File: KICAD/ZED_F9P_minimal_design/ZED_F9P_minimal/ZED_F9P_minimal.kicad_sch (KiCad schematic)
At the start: 2 parts, among them IC1 ZED-F9P-15B

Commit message: Update ZED_F9P_minimal.kicad_sch
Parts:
- added AE1: Antenna_Shield, symbol Device:Antenna_Shield
- added C2: 100nf_16V, symbol Device:C
- added C3: 11pF, symbol Device:C
- added C4: 1µF, Capacitor_SMD:C_0201_0603Metric, symbol Device:C
- added D1: LED, symbol Device:LED
- added D2: D_Zener, symbol Device:D_Zener
- added D3: D_TVS, symbol Device:D_TVS
- added FB1: 120ohm 300mA, symbol Device:FerriteBead
- added L1: 0.01 µH, symbol Device:L
- added R1: 10 Ohm, symbol Device:R
- added R2: 8.2ohm, symbol Device:R
- added R3: R, symbol Device:R
- added U1: NCV8705ML33TCG, DFNW8-3x3_ONS, symbol Voltage regulator:NCV8705ML33TCG
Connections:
- net +3.3V: now also FB1.2, U1.5 (EN), U1.8 (IN); no longer IC1.33 (VCC_1), IC1.34 (VCC_2), IC1.36 (V_BCKP)
- net GND: now also AE1.2 (Shield), C2.2, C3.2, C4.2, D1.1 (K), D2.2 (A), D3.1 (A1), U1.4 (GND)
- net at IC1.20 (RTK_STAT): now also R3.2
- net at IC1.39 (USB_DM): now also IC1.40 (USB_DP)
- net Antenna: no longer names the net of IC1.2 (RF_IN)
- net Antenna: now also C3.1, R2.2
- new net: D1.2 (A), R3.1
- new net: AE1.1 (A), D2.1 (K), D3.2 (A2), L1.1, R2.1
- new net: C4.1, IC1.33 (VCC_1), IC1.34 (VCC_2), U1.1 (OUT)
- new net: C2.1, L1.2, R1.2
- new net: FB1.1, R1.1
- no-connect marks 0 -> 29
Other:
- note added: "(input/output)- USB DATA"
- note added: "-output Sortie timer (si on veut ssynchro des choses dessus)"
- note added: "D_SEL=1 I2C_DATA / D_SEL=0 SPI Chip Select (Input/Output)- D_SEL=1 I2C_CLK / D_SEL=0 SPI_CLK (Input/Output)-"
- note added: "Etat du registre TX output- (cf p.87)buffer full ou ready for data"
- note added: "RESET du F9P, supr ttes les infos et cold start,en dernier recours uniquement input- état bas pdt 100ms pour trigger le reset"
- note added: "adaptation alimentation"
- note added: "détermination de D_SEL (input)-"
- note added: "filtre RC 1.76GHz"
- note added: "input UART from chip output"
- note added: "output- D_SEL=0 SPI_SD D_SEL=1 UART from host input-"
- note added: "protections ESD"
- note added: "statut RTK : off = fixed clignote = reçois/corrige on = pas de corrections"
- note removed: "IL faut proteger l'antenne ESD"
- moved on the sheet: IC1

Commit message: work on schematic and footprint
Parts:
- removed AE1: Antenna_Shield, symbol Device:Antenna_Shield
- removed FB1: 120ohm 300mA, symbol Device:FerriteBead
- added C5: 2µF, 2_2uF:CAPC1608X90, symbol Device:C
- added J1: Conn_Coaxial_Small, SMA:RFSOLUTIONS_CON-SMA-EDGE-S, symbol Connector:Conn_Coaxial_Small
- added R4: 120, symbol Device:R
- C1, C4: footprint Capacitor_SMD:C_0201_0603Metric -> 1uF:YAG_CC0603_YAG
- C2: footprint (none) -> 0_1uF:YAG_CC0603_YAG
- C3: footprint (none) -> 11pF:CAPC1608X90
- D1: value LED -> EASR3216RA0
- L1: footprint (none) -> 0_01uH:STA_RMCF1206_STP
- R1, R2: footprint (none) -> 10_Ohm:RC0402N_YAG
- R3: value R -> 330
- U1: footprint DFNW8-3x3_ONS -> LM5168F:DFNW8-3x3_ONS
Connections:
- net +3.3V: now also IC1.36 (V_BCKP), C5.1
- net GND: now also C5.2, J1.2 (Ext), R4.2
- net at D1.2 (A), R3.1: now also R4.1
- net RF_IN: now reaches D2.1 (K), D3.2 (A2), L1.1, R2.1
- net RF_IN: now also C3.1, IC1.2 (RF_IN), R2.2, J1.1 (In)
- net UART_RX: now reaches IC1.26 (RXD2)
- net UART_TX: now reaches IC1.27 (TXD2)
- net TIMER: now reaches IC1.53 (TIMEPULSE)
- net VCC_RF: now reaches IC1.7 (VCC_RF)
- net VCC_RF: now also R1.2
- net at C2.1, L1.2: now also R1.1; no longer R1.2
- no-connect marks 29 -> 28
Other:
- moved on the sheet: C2, C3, D1, D2, D3, L1, R2

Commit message: commit  update
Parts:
- removed R3: 330, symbol Device:R
- added R5: 330, 330_ohm:RC0603N_YAG, symbol Device:R
- added TP1, TP2, TP3, TP4, TP5: TestPoint, symbol Connector:TestPoint
- C1, C4: value 1µF -> 10µF
- R4: footprint (none) -> 120ohm:RC0805N_YAG
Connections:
- net GND: now also TP5.1
- net RF_IN: now also TP1.1, TP3.1
- net VCC_RF: now also TP2.1
- net at D1.2 (A), R4.1: now also R5.2
- net at IC1.20 (RTK_STAT): now also R5.1
- net at C4.1, IC1.33 (VCC_1), IC1.34 (VCC_2)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: now also TP4.1
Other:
- note added: "alimentation antenne en externe from 3.0V to 5.5V with 45mA"
- note added: "contacter ublox pour model PSPICE de la puce"
- moved on the sheet: D1, R4

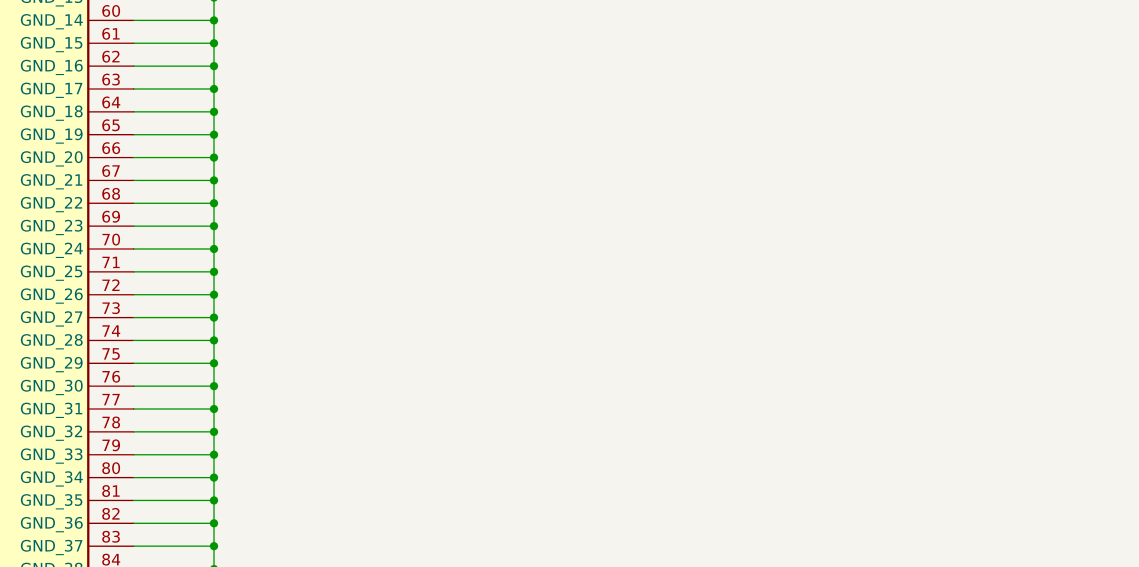
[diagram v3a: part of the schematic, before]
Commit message: TODO UART modification
Les PORTs UART DOIVENT etre déplacer sur les PIN 42 et 43 Pour utiliser UART 1 et non 2\nUART 2 a des fonctionaliser en moins
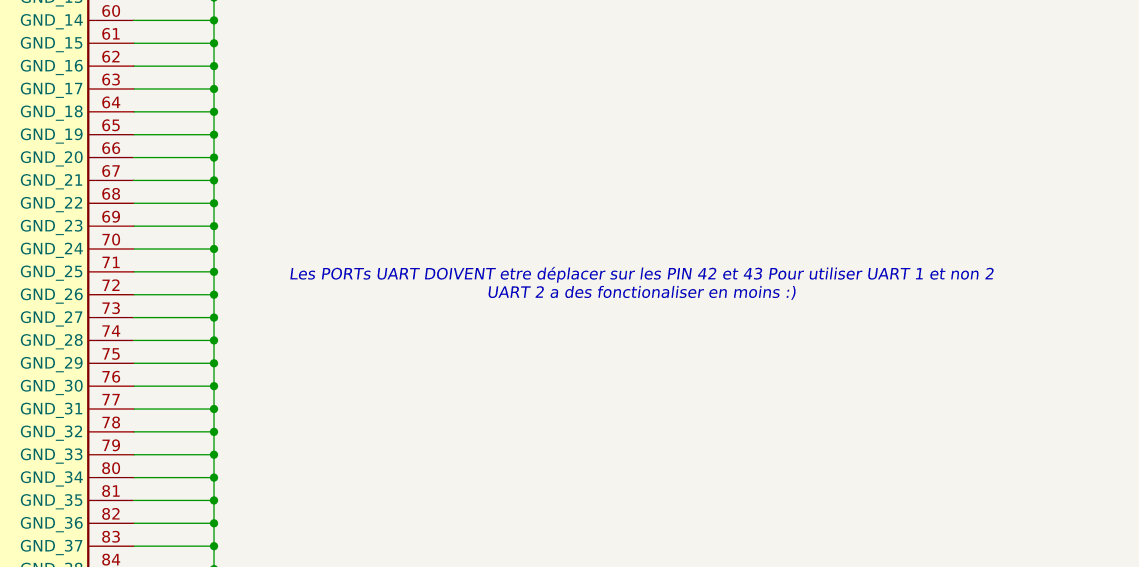
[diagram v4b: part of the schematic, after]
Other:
- note added: "Les PORTs UART DOIVENT etre déplacer sur les PIN 42 et 43 Pour utiliser UART 1 et non 2 UART 2 a des fonctionaliser en moins :)"
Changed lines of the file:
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@@
+		)
+	)
+	(text "Les PORTs UART DOIVENT etre déplacer sur les PIN 42 et 43 Pour utiliser UART 1 et non 2\nUART 2 a des fonctionaliser en moins :)"
+		(exclude_from_sim no)
+		(at 239.268 81.534 0)
+		(effects
+			(font
+				(size 1.27 1.27)
+				(italic yes)
+			)
 		)
 	)
